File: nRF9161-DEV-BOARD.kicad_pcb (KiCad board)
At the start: 4 copper layers, 120 x 80 mm, 103 parts, among them J1 VIN_3V0-5V5, J10 SPI0, J11 I2C0, J12 GPIO_P0.00-15, J13 GPIO_P0.16-31, J14 RFFE_MAGPIO, J15 COEX, J16 I2S, J17 PDM, J18 ADC_AIN0-7, J2 U.FL_LTE_NR+, J3 SWF_LTE, J5 U.FL_GNSS, J6 SWF_GNSS, J7 nanoSIM_4FF, J8 SWD_10pin, J9 UART0, SW1 DISABLE, SW2 RESET, SW3 USER, U1 NRF9161-LACA-R7, U2 TLV73330PDBV, U3 TPS22919DCKR, U4 TPD3F303DPV

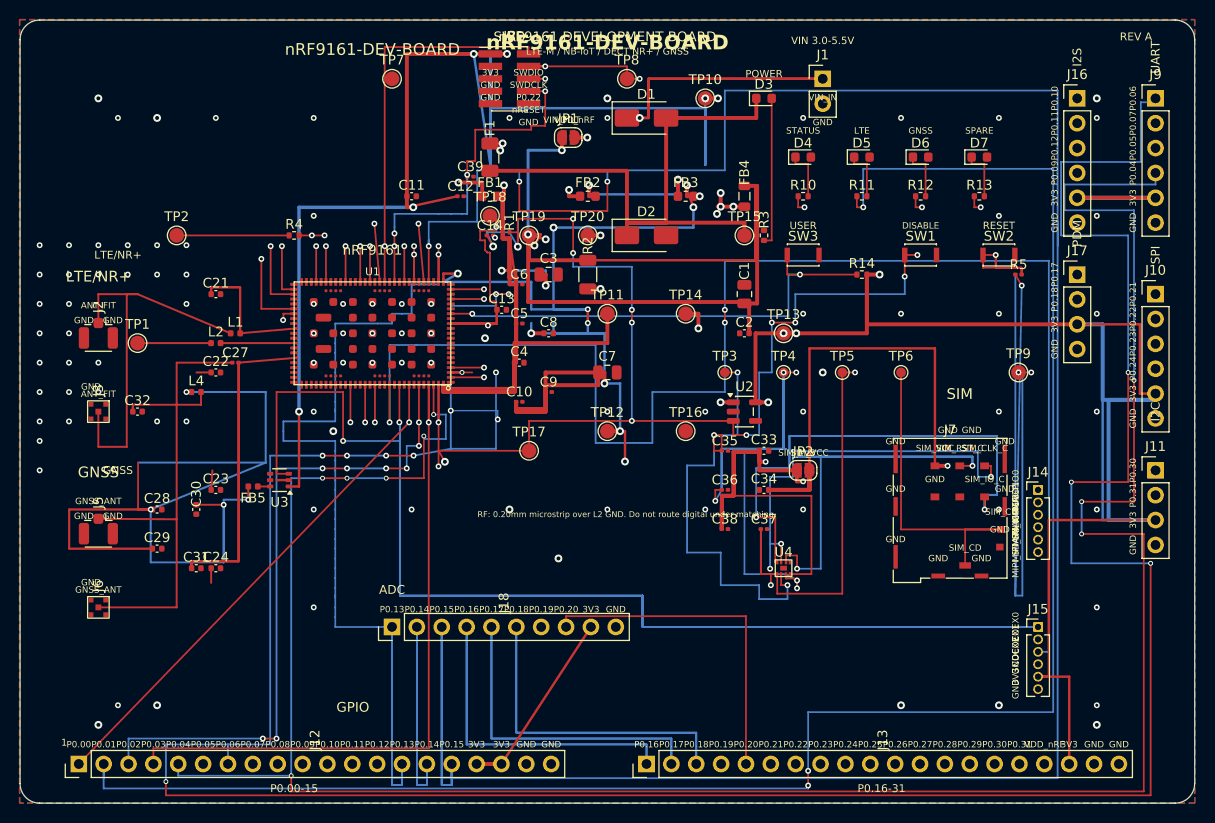
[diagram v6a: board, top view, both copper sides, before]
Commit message: PCB pass30j: finish P0.08 to J12.9; unconnected 77→76
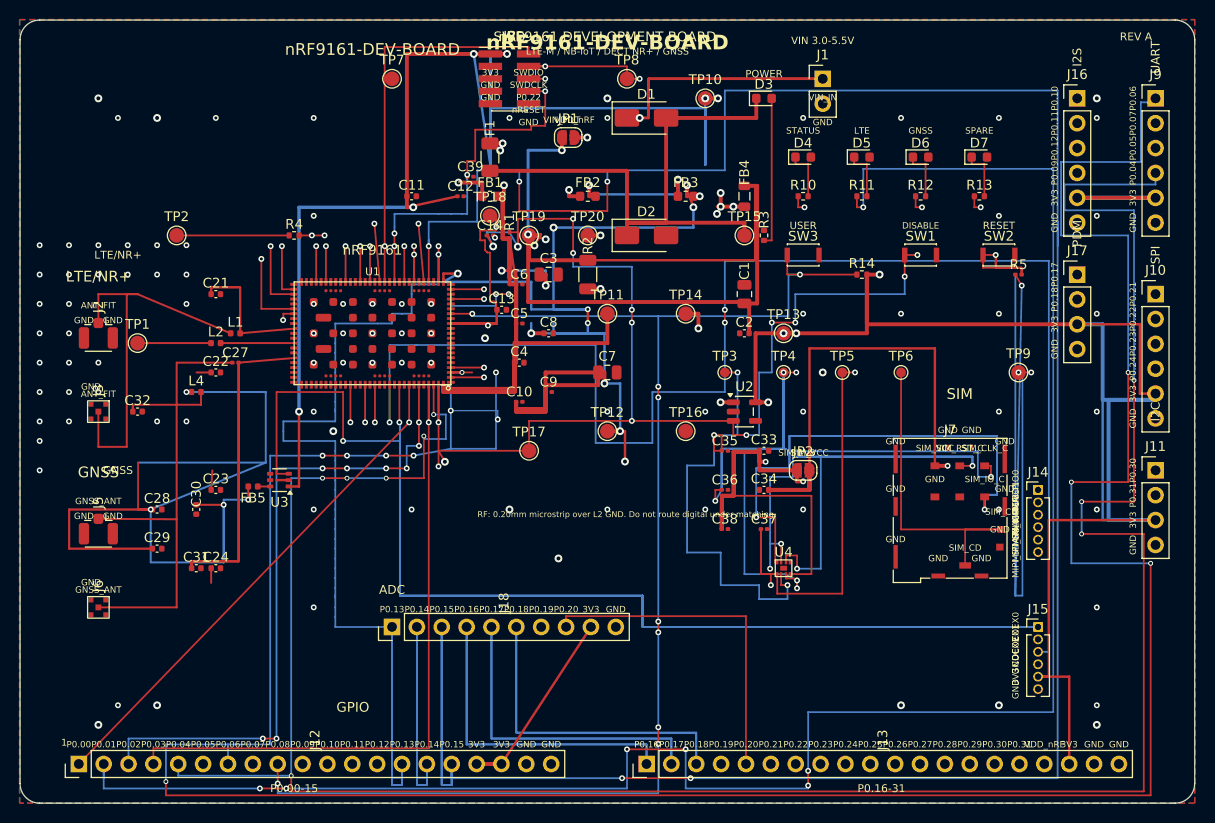
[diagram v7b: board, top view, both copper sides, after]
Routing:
- net P0.08: track 49.3 -> 139.9 mm, vias 2 -> 9
- net P0.01: track 189.4 -> 197.4 mm, vias 3 -> 7
- net P0.15: vias 3 -> 5
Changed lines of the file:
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@@
 	)
 	(segment
+		(start 62 74.5)
+		(end 68 74.5)
+		(width 0.18)
+		(layer "F.Cu")
+		(net 32)
+	)
+	(segment
 		(start 80.51 76.7)
 		(end 80.51 78.2)
@@
 		(net 32)
 	)
+	(segment
+		(start 24.5 78.5)
+		(end 27.2 78.5)
+		(width 0.18)
+		(layer "F.Cu")
+		(net 32)
+	)
 	(via
 		(at 80.51 76.7)
@@
 	)
 	(via
+		(at 62 74.5)
+		(size 0.6)
+		(drill 0.3)
+		(layers "F.Cu" "B.Cu")
+		(net 32)
+	)
+	(via
+		(at 27.2 78.5)
+		(size 0.6)
+		(drill 0.3)
+		(layers "F.Cu" "B.Cu")
+		(net 32)
+	)
+	(via
 		(at 80.51 78.2)
 		(size 0.6)
@@
 		(net 32)
 	)
+	(via
+		(at 24.5 78.5)
+		(size 0.6)
+		(drill 0.3)
+		(layers "F.Cu" "B.Cu")
+		(net 32)
+	)
+	(via
+		(at 68 74.5)
+		(size 0.6)
+		(drill 0.3)
+		(layers "F.Cu" "B.Cu")
+		(net 32)
+	)
+	(segment
+		(start 8.54 78.5)
+		(end 24.5 78.5)
+		(width 0.18)
+		(layer "B.Cu")
+		(net 32)
+	)
 	(segment
 		(start 105.55 15.2)
@@
 	)
 	(segment
+		(start 68 78.5)
+		(end 80.51 78.5)
+		(width 0.18)
+		(layer "B.Cu")
+		(net 32)
+	)
+	(segment
 		(start 8.54 78.5)
 		(end 8.54 76)
@@
 	)
 	(segment
-		(start 80.51 78.5)
-		(end 8.54 78.5)
+		(start 68 74.5)
+		(end 68 78.5)
 		(width 0.18)
 		(layer "B.Cu")
@@
 	)
 	(segment
+		(start 27.2 78.5)
+		(end 62 78.5)
+		(width 0.18)
+		(layer "B.Cu")
+		(net 32)
+	)
+	(segment
 		(start 80.51 78.2)
 		(end 80.51 78.5)
@@
 	)
 	(segment
+		(start 62 78.5)
+		(end 62 74.5)
+		(width 0.18)
+		(layer "B.Cu")
+		(net 32)
+	)
+	(segment
 		(start 80.51 70.7)
 		(end 80.51 76.7)
@@
 	)
 	(segment
+		(start 61.5 77.45)
+		(end 68.5 77.45)
+		(width 0.18)
+		(layer "F.Cu")
+		(net 42)
+	)
+	(segment
 		(start 51 16.5)
 		(end 51 19.5)
@@
 	)
 	(via
+		(at 61.5 77.45)
+		(size 0.6)
+		(drill 0.3)
+		(layers "F.Cu" "B.Cu")
+		(net 42)
+	)
+	(via
+		(at 68.5 77.45)
+		(size 0.6)
+		(drill 0.3)
+		(layers "F.Cu" "B.Cu")
+		(net 42)
+	)
+	(via
 		(at 51 16.5)
 		(size 0.6)
@@
 	)
 	(segment
+		(start 44.1 77.45)
+		(end 61.5 77.45)
+		(width 0.18)
+		(layer "B.Cu")
+		(net 42)
+	)
+	(segment
 		(start 44.1 76)
 		(end 44.1 78.15)
@@
 	)
 	(segment
-		(start 106 77.45)
-		(end 44.1 77.45)
-		(width 0.18)
-		(layer "B.Cu")
-		(net 42)
-	)
-	(segment
 		(start 46.7 20.6)
 		(end 46.7 15.35)
@@
 	)
 	(segment
+		(start 68.5 77.45)
+		(end 106 77.45)
+		(width 0.18)
+		(layer "B.Cu")
+		(net 42)
+	)
+	(segment
 		(start 26.75 27.5)
 		(end 26.75 23.1)
@@
 	)
 	(segment
+		(start 65.2 72.25)
+		(end 65.2 73.95)
+		(width 0.18)
+		(layer "F.Cu")
+		(net 61)
+	)
+	(segment
 		(start 44 30)
 		(end 46.2 30)
@@
 	)
 	(segment
+		(start 26.32 78)
+		(end 26.32 76)
+		(width 0.18)
+		(layer "F.Cu")
+		(net 61)
+	)
+	(segment
+		(start 65.2 37.45)
+		(end 65.2 38.55)
+		(width 0.18)
+		(layer "F.Cu")
+		(net 61)
+	)
+	(segment
+		(start 65.2 61.45)
+		(end 65.2 62.55)
+		(width 0.18)
+		(layer "F.Cu")
+		(net 61)
+	)
+	(segment
 		(start 78.375 24)
 		(end 78.375 26)
@@
 	)
 	(via
+		(at 65.2 73.95)
+		(size 0.6)
+		(drill 0.3)
+		(layers "F.Cu" "B.Cu")
+		(net 61)
+	)
+	(via
+		(at 65.2 62.55)
+		(size 0.6)
+		(drill 0.3)
+		(layers "F.Cu" "B.Cu")
+		(net 61)
+	)
+	(via
+		(at 65.2 72.25)
+		(size 0.6)
+		(drill 0.3)
+		(layers "F.Cu" "B.Cu")
+		(net 61)
+	)
+	(via
+		(at 65.2 61.45)
+		(size 0.6)
+		(drill 0.3)
+		(layers "F.Cu" "B.Cu")
+		(net 61)
+	)
+	(via
 		(at 79.675 26)
 		(size 0.6)
@@
 	)
 	(via
+		(at 65.2 38.55)
+		(size 0.6)
+		(drill 0.3)
+		(layers "F.Cu" "B.Cu")
+		(net 61)
+	)
+	(via
 		(at 46.2 30)
 		(size 0.6)
@@
 		(net 61)
 	)
+	(via
+		(at 26.32 78)
+		(size 0.6)
+		(drill 0.3)
+		(layers "F.Cu" "B.Cu")
+		(net 61)
+	)
+	(via
+		(at 65.2 37.45)
+		(size 0.6)
+		(drill 0.3)
+		(layers "F.Cu" "B.Cu")
+		(net 61)
+	)
+	(segment
+		(start 26.32 79)
+		(end 26.32 78)
+		(width 0.18)
+		(layer "B.Cu")
+		(net 61)
+	)
 	(segment
 		(start 78.5 26)
@@
 	)
 	(segment
+		(start 65.2 73.95)
+		(end 65.2 79)
+		(width 0.18)
+		(layer "B.Cu")
+		(net 61)
+	)
+	(segment
 		(start 46.2 30)
 		(end 46.2 30.25)
@@
 	)
 	(segment
+		(start 65.2 62.55)
+		(end 65.2 72.25)
+		(width 0.18)
+		(layer "B.Cu")
+		(net 61)
+	)
+	(segment
+		(start 65.2 38.55)
+		(end 65.2 61.45)
+		(width 0.18)
+		(layer "B.Cu")
+		(net 61)
+	)
+	(segment
+		(start 65.2 30.25)
+		(end 65.2 37.45)
+		(width 0.18)
+		(layer "B.Cu")
+		(net 61)
+	)
+	(segment
 		(start 78.5 30.25)
 		(end 78.5 26)
 		(width 0.18)
 		(layer "B.Cu")
+		(net 61)
+	)
+	(segment
+		(start 65.2 79)
+		(end 26.32 79)
+		(width 0.18)
+		(layer "B.Cu")
